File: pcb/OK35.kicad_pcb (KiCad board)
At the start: 2 copper layers, 133.3 x 116.2 mm, 81 parts, among them SW1 SW_SPST, SW10 SW_SPST, SW11 SW_SPST, SW12 SW_SPST, SW13 SW_SPST, SW14 SW_SPST, SW15 SW_SPST, SW16 SW_SPST, SW17 SW_SPST, SW18 SW_SPST, SW19 SW_SPST, SW2 SW_SPST, SW20 SW_SPST, SW21 SW_SPST, SW22 SW_SPST, SW23 SW_SPST, SW24 SW_SPST, SW25 SW_SPST, SW26 SW_SPST, SW27 SW_SPST, SW28 SW_SPST, SW29 SW_SPST, SW3 SW_SPST, SW30 SW_SPST, SW31 SW_SPST, SW32 SW_SPST, SW33 SW_SPST, SW34 SW_SPST, SW35 SW_SPST, SW36 SW_SPST, SW37 SW_SPST, SW4 SW_SPST, SW5 SW_SPST, SW6 SW_SPST, SW7 SW_SPST, SW8 SW_SPST, SW9 SW_SPST, U1 TRRS, U2 ProMicro

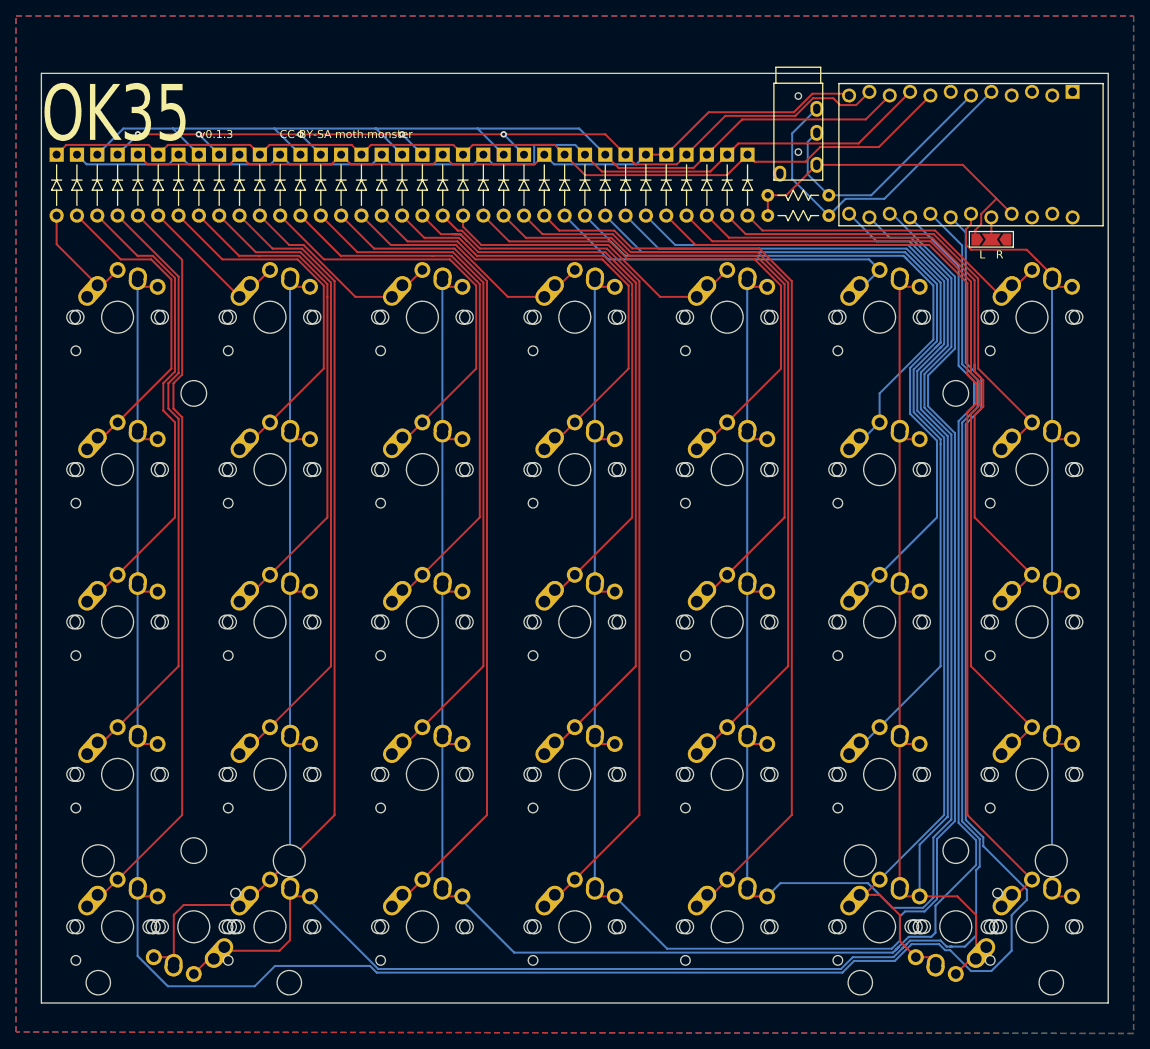
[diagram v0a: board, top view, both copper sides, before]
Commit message: v0.1.3 was bad
This reverts commit 27f9da0c8f8c043d86356701b4d41a0e5f33df05.
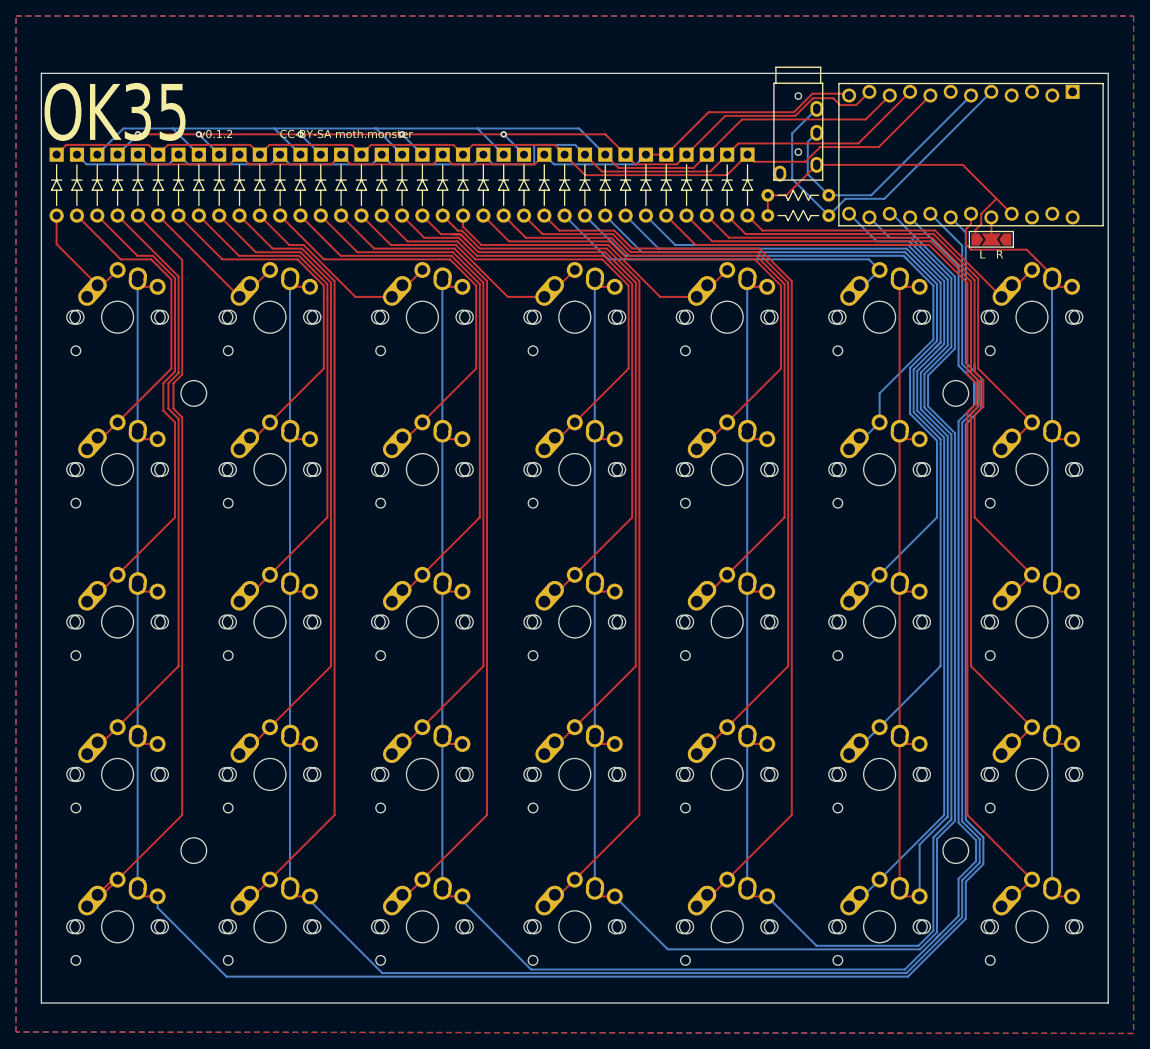
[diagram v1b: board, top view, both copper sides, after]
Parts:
- removed SW36, SW37: SW_SPST, keebio:MX-Alps-Choc-2U
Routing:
- net Col1: track 293.8 -> 271.9 mm
- net Col0: track 312.6 -> 291.2 mm
- net Net-(D30-Pad2): track 116.2 -> 98.6 mm
- net Col5: track 203.8 -> 187.3 mm
- net Net-(D34-Pad2): track 140.3 -> 126.8 mm
- net Col4: track 208.0 -> 212.9 mm
- net Net-(D29-Pad2): track 95.3 -> 98.0 mm
- net Col2: track 250.7 -> 253.0 mm
- net Col3: track 230.4 -> 231.1 mm
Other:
- board text added: "v0.1.2"
- board text removed: "v0.1.3"

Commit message: v0.1.3 - standard 2u switch options
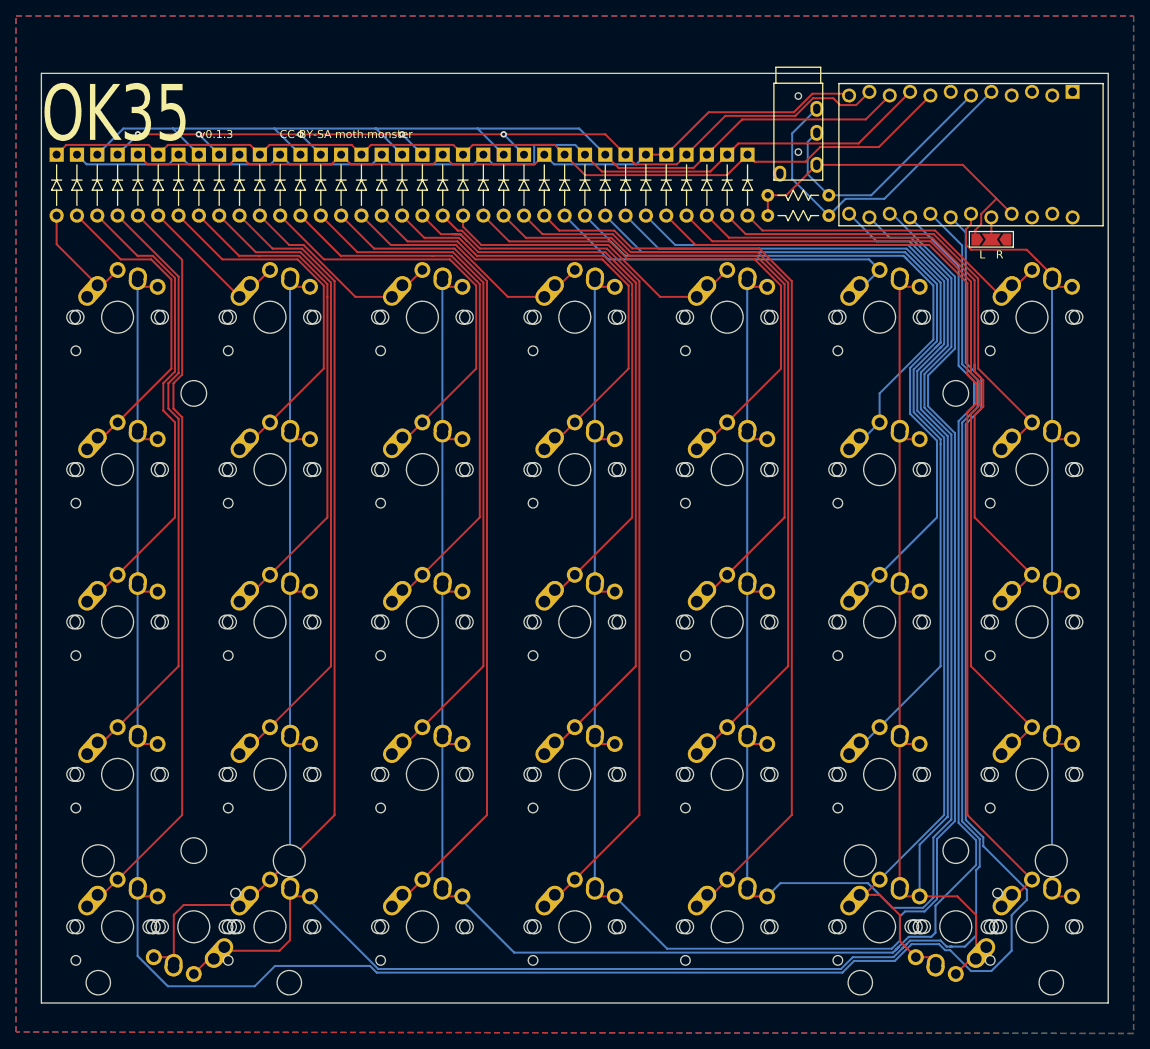
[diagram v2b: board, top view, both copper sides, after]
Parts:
- added SW36: SW_SPST, keebio:MX-Alps-Choc-2U, F.Cu at (98.4, 139.2)
- added SW37: SW_SPST, keebio:MX-Alps-Choc-2U, F.Cu at (193.7, 139.2)
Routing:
- net Col1: track 271.9 -> 293.8 mm
- net Col0: track 291.2 -> 312.6 mm
- net Net-(D30-Pad2): track 98.6 -> 116.2 mm
- net Col5: track 187.3 -> 203.8 mm
- net Net-(D34-Pad2): track 126.8 -> 140.3 mm
- net Col4: track 212.9 -> 208.0 mm
- net Net-(D29-Pad2): track 98.0 -> 95.3 mm
- net Col2: track 253.0 -> 250.7 mm
- net Col3: track 231.1 -> 230.4 mm
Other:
- board text added: "v0.1.3"
- board text removed: "v0.1.2"
